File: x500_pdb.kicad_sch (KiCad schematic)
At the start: 33 parts, among them IC1 LM21305SQ_NOPB, J1 Conn_01x02, J2 Conn_01x02, J3 Conn_01x02, J4 Conn_01x02

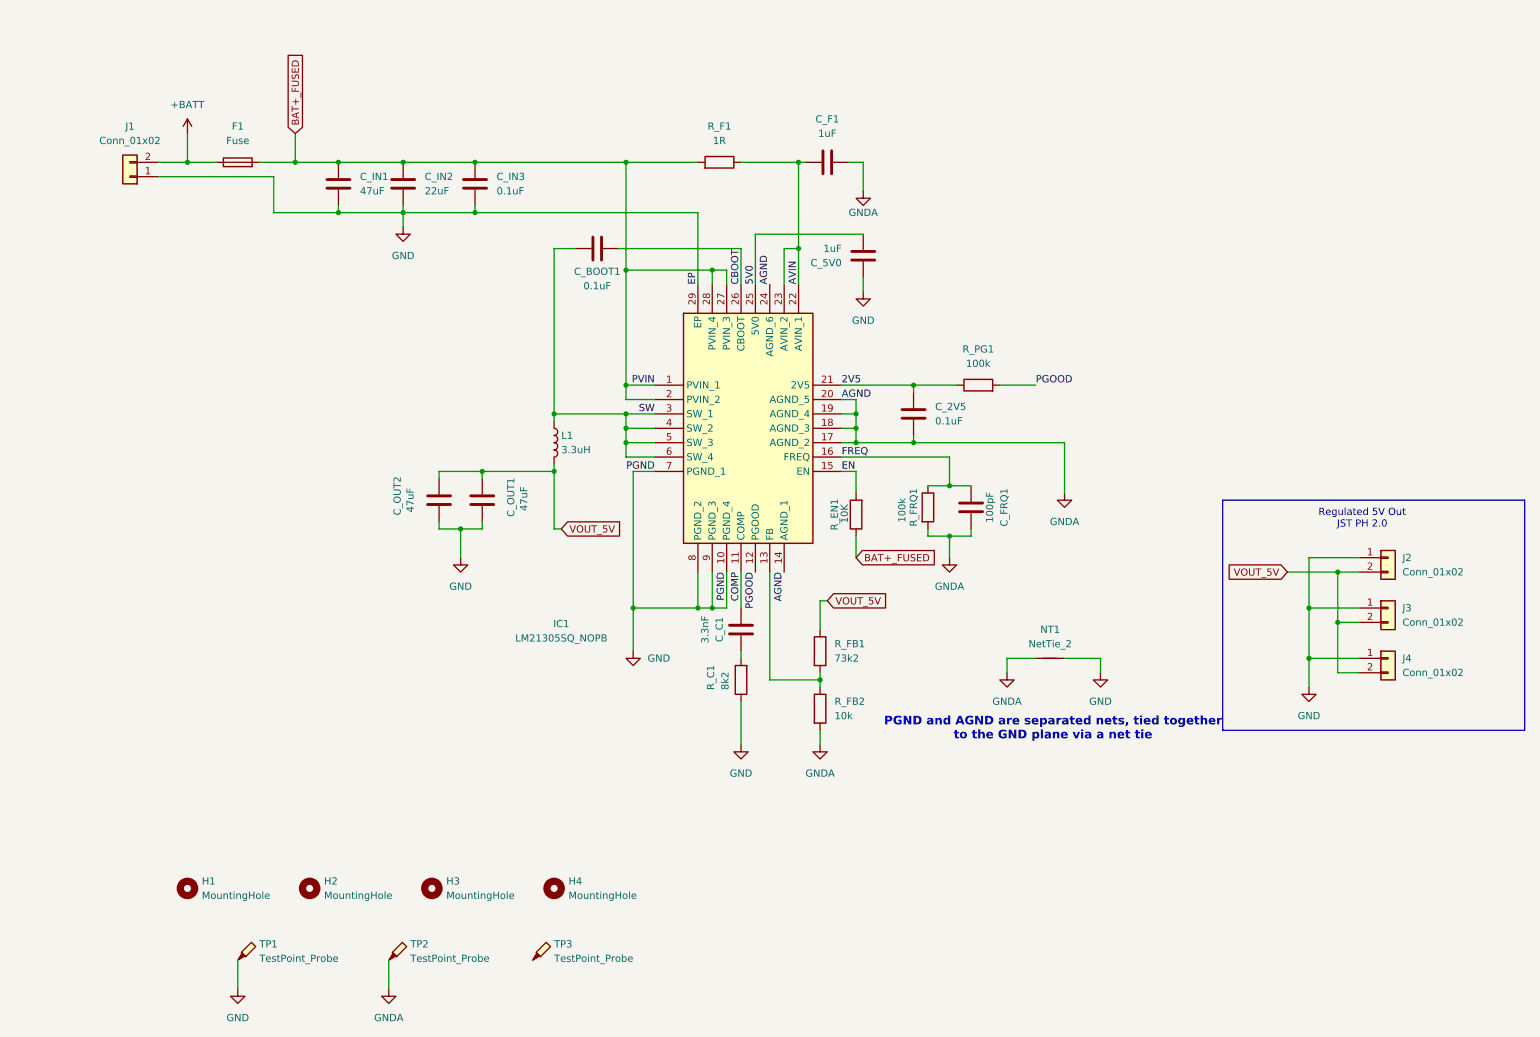
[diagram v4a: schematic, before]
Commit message: Change mounting holes to plated ones
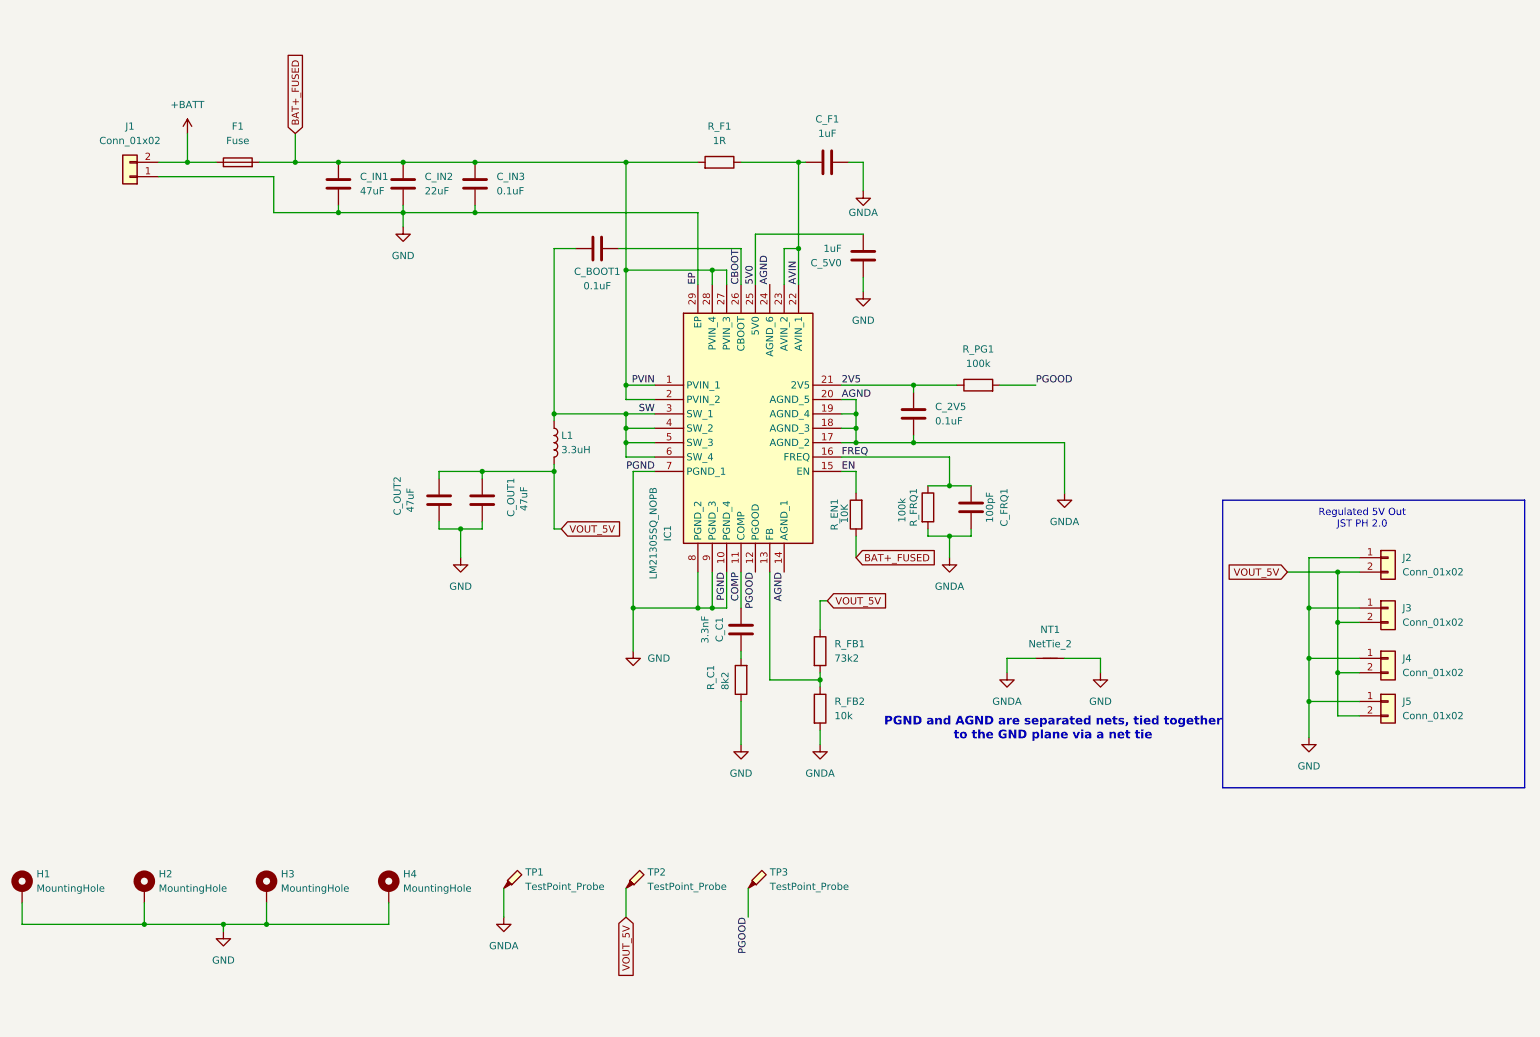
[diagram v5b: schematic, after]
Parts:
- added J5: Conn_01x02, Connector_JST:JST_PH_S2B-PH-K_1x02_P2.00mm_Horizontal, symbol Connector_Generic:Conn_01x02
- H1, H2, H3, H4: footprint MountingHole:MountingHole_3.2mm_M3 -> MountingHole:MountingHole_3.2mm_M3_DIN965_Pad_TopBottom; symbol Mechanical:MountingHole -> Mechanical:MountingHole_Pad
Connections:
- net GND: now also H1.1, H2.1, H3.1, H4.1, J5.1 (Pin_1); no longer TP1.1
- net GNDA: now also TP1.1; no longer TP2.1
- net PGOOD: now also TP3.1
- net VOUT_5V: now also TP2.1, J5.2 (Pin_2)
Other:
- moved on the sheet: TP1, TP2, TP3

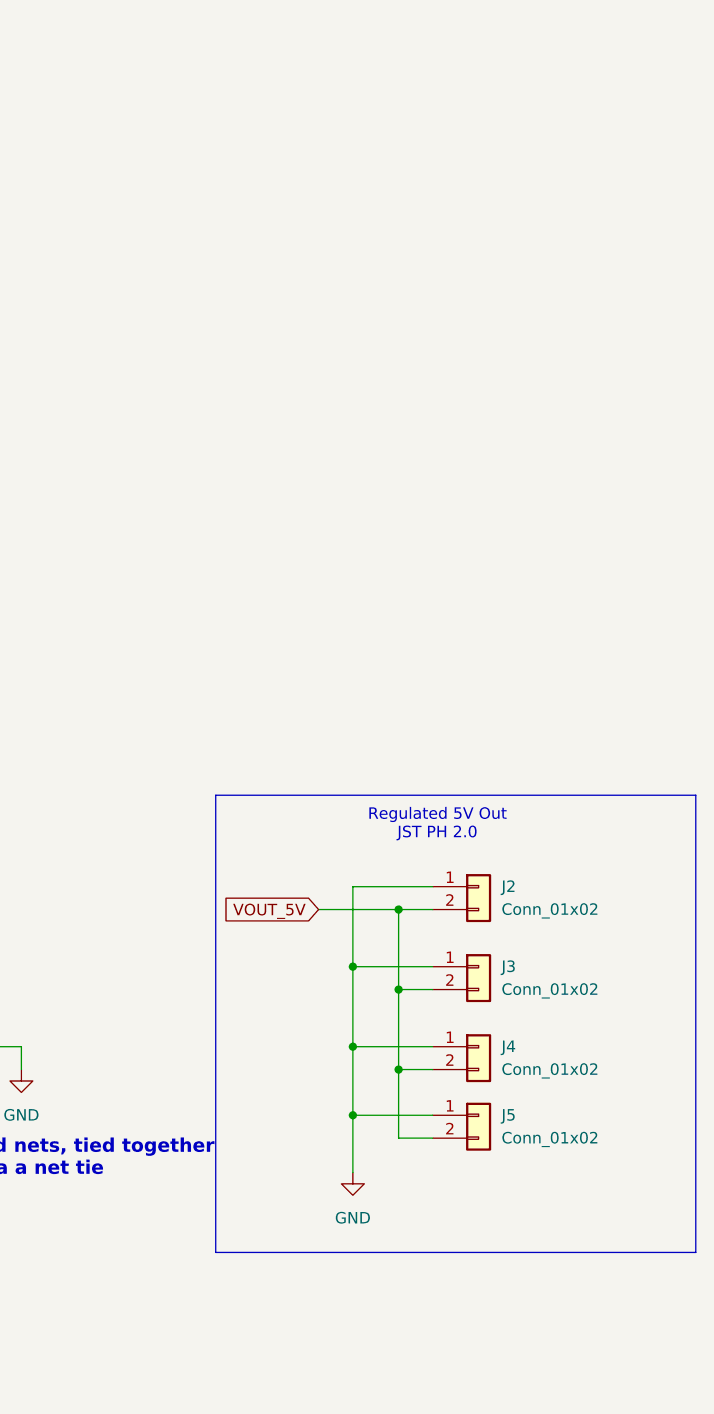
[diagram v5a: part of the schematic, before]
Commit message: Adding BAT_FUSED Outputs
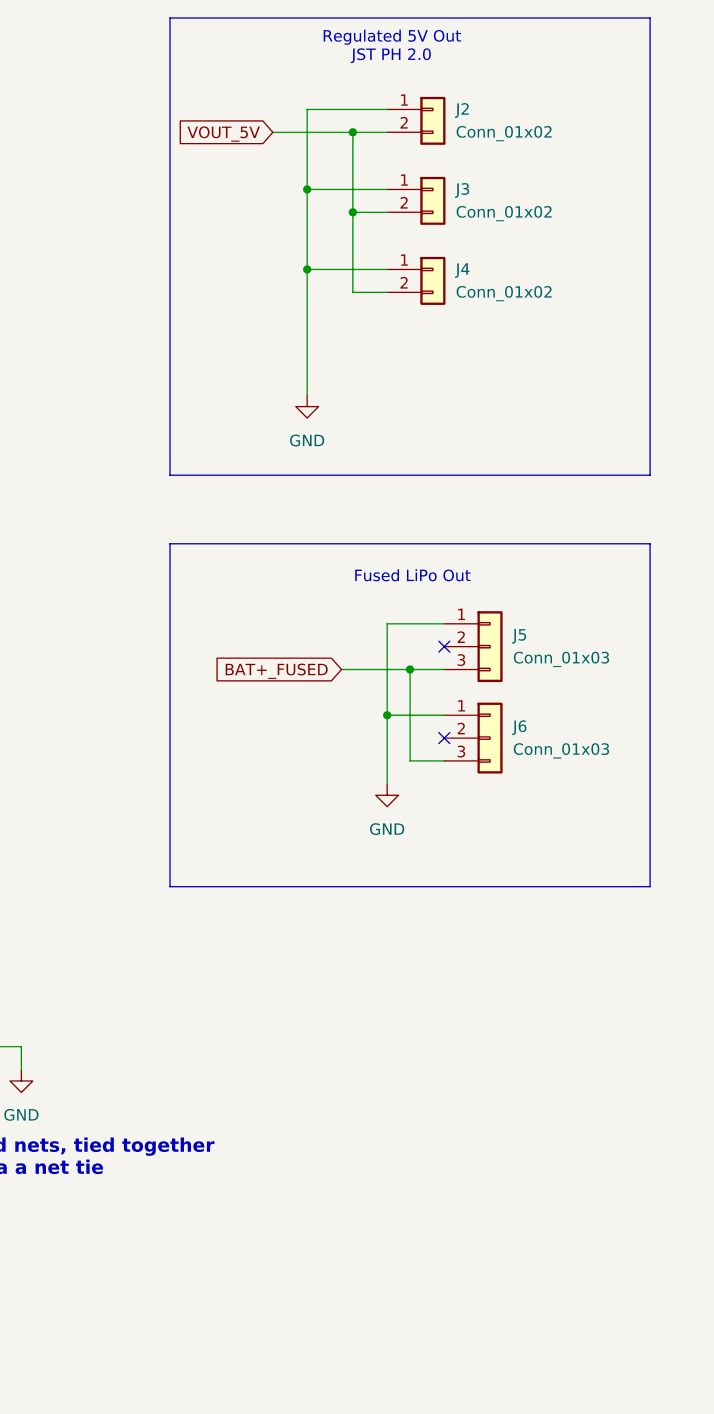
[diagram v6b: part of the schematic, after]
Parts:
- removed J5: Conn_01x02, Connector_JST:JST_PH_S2B-PH-K_1x02_P2.00mm_Horizontal, symbol Connector_Generic:Conn_01x02
- added J5, J6: Conn_01x03, Connector_JST:JST_PH_S3B-PH-K_1x03_P2.00mm_Horizontal, symbol Connector_Generic:Conn_01x03
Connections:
- net BAT+_FUSED: now also J5.3 (Pin_3), J6.3 (Pin_3)
- net GND: now also J5.1 (Pin_1), J6.1 (Pin_1)
- no-connect marks 0 -> 2
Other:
- note added: "Fused LiPo Out"
- moved on the sheet: J2, J3, J4

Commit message: 1.0-RC3 Assigning Mouser Pt.No.
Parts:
- C_IN1: Mouser Part Number (none) -> 80-T495D476K25ATE120
- C_IN2: Mouser Part Number (none) -> 81-GRM32ER61E226KE15
- C_IN3: Mouser Part Number (none) -> 81-GCJ31MR71E104KA1L
- R_FRQ1, R_PG1: Mouser Part Number (none) -> 594-MCT06030C1003FP5
- TP1, TP2, TP3: now left out of the parts list
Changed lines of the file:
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@@
 		(unit 1)
 		(exclude_from_sim no)
-		(in_bom yes)
+		(in_bom no)
 		(on_board yes)
 		(dnp no)
@@
 			)
 		)
+		(property "Mouser Part Number" "81-GRM32ER61E226KE15"
+			(at 83.82 48.26 0)
+			(effects
+				(font
+					(size 1.27 1.27)
+				)
+				(hide yes)
+			)
+		)
 		(pin "1"
 		)
@@
 			)
 		)
+		(property "Mouser Part Number" "594-MCT06030C1003FP5"
+			(at 185.42 83.82 90)
+			(effects
+				(font
+					(size 1.27 1.27)
+				)
+				(hide yes)
+			)
+		)
 		(pin "2"
 		)
@@
 			)
 		)
+		(property "Mouser Part Number" "81-GCJ31MR71E104KA1L"
+			(at 96.52 48.26 0)
+			(effects
+				(font
+					(size 1.27 1.27)
+				)
+				(hide yes)
+			)
+		)
 		(pin "1"
 		)
@@
 			)
 		)
+		(property "Mouser Part Number" "594-MCT06030C1003FP5"
+			(at 176.53 105.41 90)
+			(effects
+				(font
+					(size 1.27 1.27)
+				)
+				(hide yes)
+			)
+		)
 		(pin "2"
 		)
@@
 		(unit 1)
 		(exclude_from_sim no)
-		(in_bom yes)
+		(in_bom no)
 		(on_board yes)
 		(dnp no)
@@
 		(unit 1)
 		(exclude_from_sim no)
-		(in_bom yes)
+		(in_bom no)
 		(on_board yes)
 		(dnp no)
@@
 			(at 72.39 48.26 0)
 			(effects
+				(font
+					(size 1.27 1.27)
+				)
+				(hide yes)
+			)
+		)
+		(property "Mouser Part Number" "80-T495D476K25ATE120"
+			(at 72.39 48.26 0)
+			(effects

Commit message: Added Mouser Part-Numbers except XT60-Connector
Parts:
- C_2V5, C_BOOT1: Mouser Part Number (none) -> 80-C0603X104J4RECAUT
- C_5V0: Mouser Part Number (none) -> 80-C0603X105J4R
- C_C1: Mouser Part Number (none) -> 581-0603YC332JAT2A
- C_F1: Mouser Part Number (none) -> 187-CL10B105KA8NNWC
- C_FRQ1: Mouser Part Number (none) -> 581-06033C101JAT4A
- C_OUT1, C_OUT2: Mouser Part Number (none) -> 81-GRM31CR61A476KE5L
- F1: Mouser Part Number (none) -> 652-SF-1206F250M-2
- J2, J3, J4: Mouser Part Number (none) -> 306-S2BPHKSLFSNPP
- J5, J6: Mouser Part Number (none) -> 306-S3BPHKSLFSN
- L1: Mouser Part Number (none) -> 652-SRP7050WA-3R3M
- R_C1: Mouser Part Number (none) -> 652-CR0603FX-8201ELF
- R_EN1: Mouser Part Number (none) -> 756-WCR1206-10KFA
- R_F1: Mouser Part Number (none) -> 667-ERJ-3GEYJ1R0V
- R_FB1: Mouser Part Number (none) -> 660-RN73H1JT7232F100
- R_FB2: Mouser Part Number (none) -> 71-CRCW060310K0FKEI
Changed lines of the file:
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@@
 		(exclude_from_sim no)
 		(in_bom yes)
-		(on_board yes)
+		(on_board no)
 		(dnp no)
 		(property "Reference" "C_OUT1"
@@
 			)
 		)
+		(property "Mouser Part Number" " 81-GRM31CR61A476KE5L "
+			(at 97.79 104.14 90)
+			(effects
+				(font
+					(size 1.27 1.27)
+				)
+				(hide yes)
+			)
+		)
 		(pin "1"
 		)
@@
 			)
 		)
+		(property "Mouser Part Number" " 306-S3BPHKSLFSN "
+			(at 259.08 97.79 0)
+			(effects
+				(font
+					(size 1.27 1.27)
+				)
+				(hide yes)
+			)
+		)
 		(pin "2"
 		)
@@
 			)
 		)
+		(property "Mouser Part Number" " 756-WCR1206-10KFA "
+			(at 163.83 106.68 90)
+			(effects
+				(font
+					(size 1.27 1.27)
+				)
+				(hide yes)
+			)
+		)
 		(pin "1"
 		)
@@
 			)
 		)
+		(property "Mouser Part Number" " 187-CL10B105KA8NNWC "
+			(at 158.75 44.45 90)
+			(effects
+				(font
+					(size 1.27 1.27)
+				)
+				(hide yes)
+			)
+		)
 		(pin "1"
 		)
@@
 		(exclude_from_sim no)
 		(in_bom yes)
-		(on_board yes)
+		(on_board no)
 		(dnp no)
 		(property "Reference" "C_OUT2"
@@
 			)
 		)
+		(property "Mouser Part Number" " 81-GRM31CR61A476KE5L "
+			(at 90.17 104.14 90)
+			(effects
+				(font
+					(size 1.27 1.27)
+				)
+				(hide yes)
+			)
+		)
 		(pin "2"
 		)
@@
 			)
 		)
+		(property "Mouser Part Number" " 660-RN73H1JT7232F100 "
+			(at 157.48 130.81 0)
+			(effects
+				(font
+					(size 1.27 1.27)
+				)
+				(hide yes)
+			)
+		)
 		(pin "2"
 		)
@@
 			)
 		)
+		(property "Mouser Part Number" " 581-06033C101JAT4A "
+			(at 184.15 105.41 90)
+			(effects
+				(font
+					(size 1.27 1.27)
+				)
+				(hide yes)
+			)
+		)
 		(pin "1"
 		)
@@
 			)
 		)
+		(property "Mouser Part Number" " 652-SRP7050WA-3R3M "
+			(at 110.49 93.98 0)
+			(effects
+				(font
+					(size 1.27 1.27)
+				)
+				(hide yes)
+			)
+		)
 		(pin "1"
 		)
@@
 			)
 		)
+		(property "Mouser Part Number" " 306-S3BPHKSLFSN "
+			(at 259.08 87.63 0)
+			(effects
+				(font
+					(size 1.27 1.27)
+				)
+				(hide yes)
+			)
+		)
 		(pin "2"
 		)
@@
 			)
 		)
+		(property "Mouser Part Number" " 306-S2BPHKSLFSNPP "
+			(at 252.73 45.72 0)
+			(effects
+				(font
+					(size 1.27 1.27)
+				)
+				(hide yes)
+			)
+		)
 		(pin "1"
 		)
@@
 			)
 		)
+		(property "Mouser Part Number" " 581-0603YC332JAT2A "
+			(at 143.51 127 90)
+			(effects
+				(font
+					(size 1.27 1.27)
+				)
+				(hide yes)
+			)
+		)
 		(pin "1"
 		)
@@
 			)
 		)
+		(property "Mouser Part Number" " 80-C0603X105J4R "
+			(at 165.1 60.96 0)
+			(effects
+				(font
+					(size 1.27 1.27)
+				)
+				(hide yes)
+			)
+		)
 		(pin "2"
 		)
@@
 			)
 		)
+		(property "Mouser Part Number" " 80-C0603X104J4RECAUT "
+			(at 173.99 88.9 0)
+			(effects
+				(font
+					(size 1.27 1.27)
+				)
+				(hide yes)
+			)
+		)
 		(pin "1"
 		)
@@
 			)
 		)
+		(property "Mouser Part Number" " 306-S2BPHKSLFSNPP "
+			(at 252.73 27.94 0)
+			(effects
+				(font
+					(size 1.27 1.27)
+				)
+				(hide yes)
+			)
+		)
 		(pin "1"
 		)
@@
 			)
 		)
+		(property "Mouser Part Number" " 306-S2BPHKSLFSNPP "
+			(at 252.73 36.83 0)
+			(effects
+				(font
+					(size 1.27 1.27)
+				)
+				(hide yes)
+			)
+		)
 		(pin "1"
 		)
@@
 			)
 		)
+		(property "Mouser Part Number" " 652-CR0603FX-8201ELF "
+			(at 143.51 135.89 90)
+			(effects
+				(font
+					(size 1.27 1.27)
+				)
+				(hide yes)
+			)
+		)
 		(pin "1"
 		)
@@
 			)
 		)
+		(property "Mouser Part Number" " 652-SF-1206F250M-2 "
+			(at 54.61 44.45 90)
+			(effects
+				(font
+					(size 1.27 1.27)
+				)
+				(hide yes)
+			)
+		)
 		(pin "1"
 		)
@@
 			)
 		)
+		(property "Mouser Part Number" " 71-CRCW060310K0FKEI "
+			(at 157.48 140.97 0)
+			(effects
+				(font
+					(size 1.27 1.27)
+				)
+				(hide yes)
+			)
+		)
 		(pin "2"
 		)
@@
 			)
 		)
+		(property "Mouser Part Number" " 667-ERJ-3GEYJ1R0V "
+			(at 139.7 44.45 90)
+			(effects
+				(font
+					(size 1.27 1.27)
+				)
+				(hide yes)
+			)
+		)
 		(pin "2"
 		)
@@
 			(effects
 				(font
+					(size 1.27 1.27)
+				)
+				(hide yes)
+			)
+		)
+		(property "Mouser Part Number" " 80-C0603X104J4RECAUT "
+			(at 118.11 59.69 90)
+			(effects
+				(font
